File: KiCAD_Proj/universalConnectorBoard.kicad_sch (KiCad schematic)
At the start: 57 parts, among them IC1 RPI_Pico_EvaluationBoard, IC2 SN74LV4052ADR, IC4 TCA9534DWR, J1 691401700003B, J10 Cheeks, J11 MD_SW1, J12 MD_SW2, J13 Motor1, J14 Motor2, J15 Extra VCC/GND, J2 Display1, J3 Display2, J4 RPI4, J5 Ledstrip2, J6 Extra MUX_UART, J7 Radar, J8 Ledstrip1, J9 Mouth, Q1 2N7002, Q2 2N7002, Q3 BSS84, SW1 SW_Push

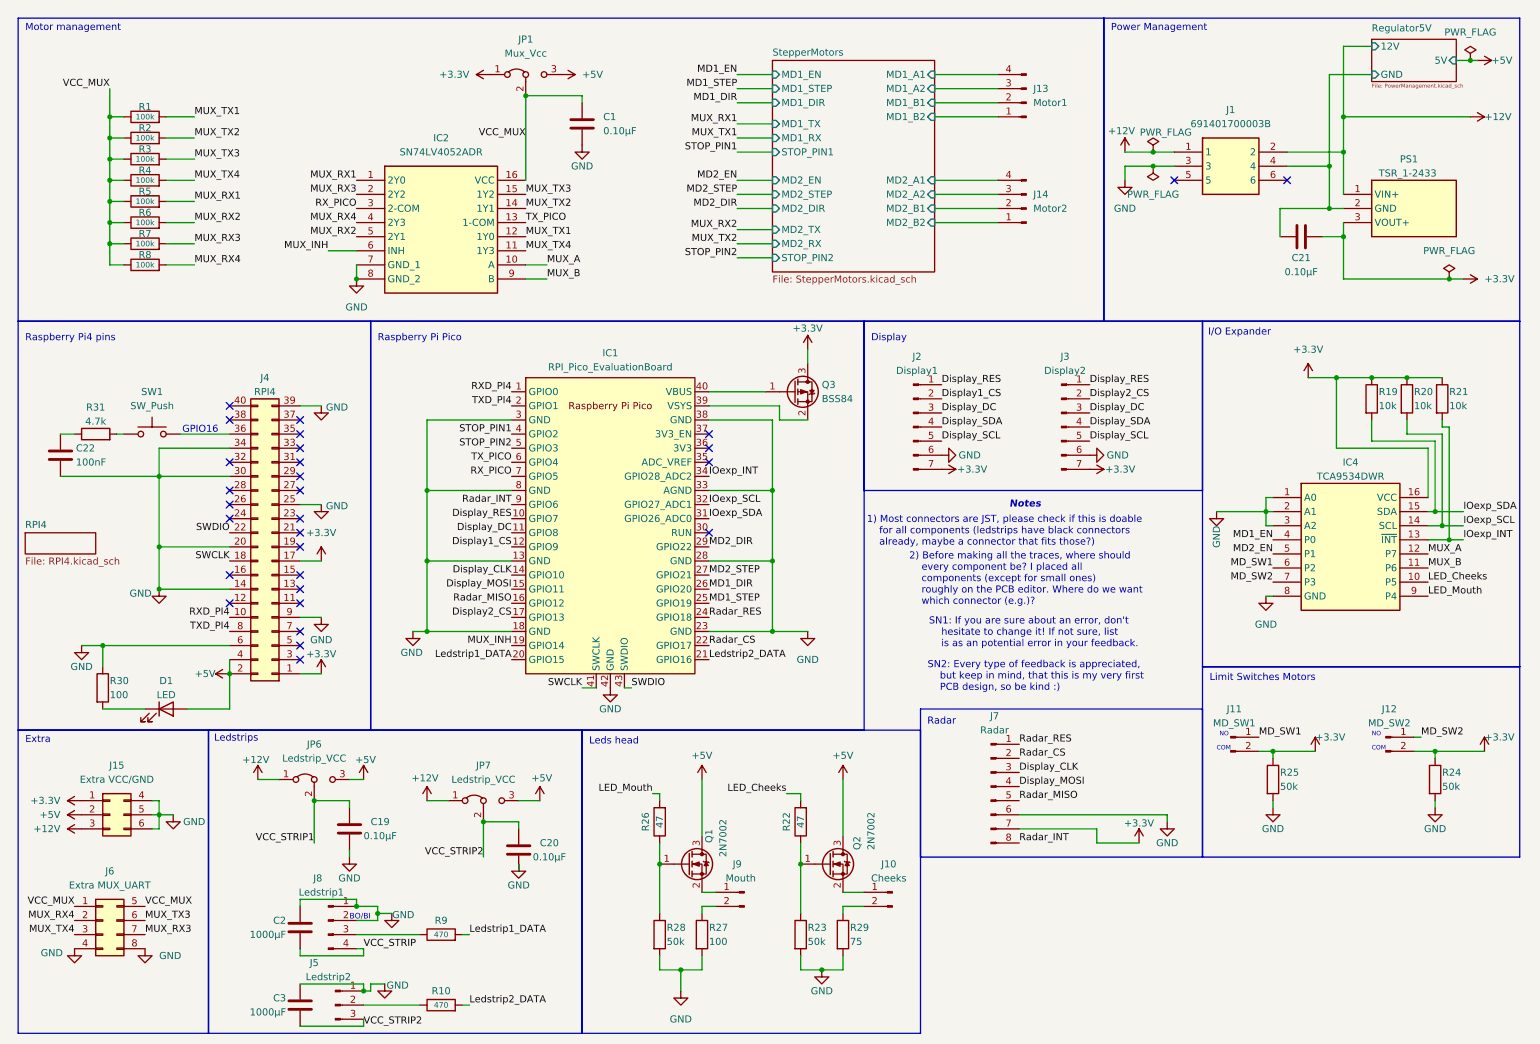
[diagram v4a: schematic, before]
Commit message: Added RPI4 footprint + headers, start of pcb designer
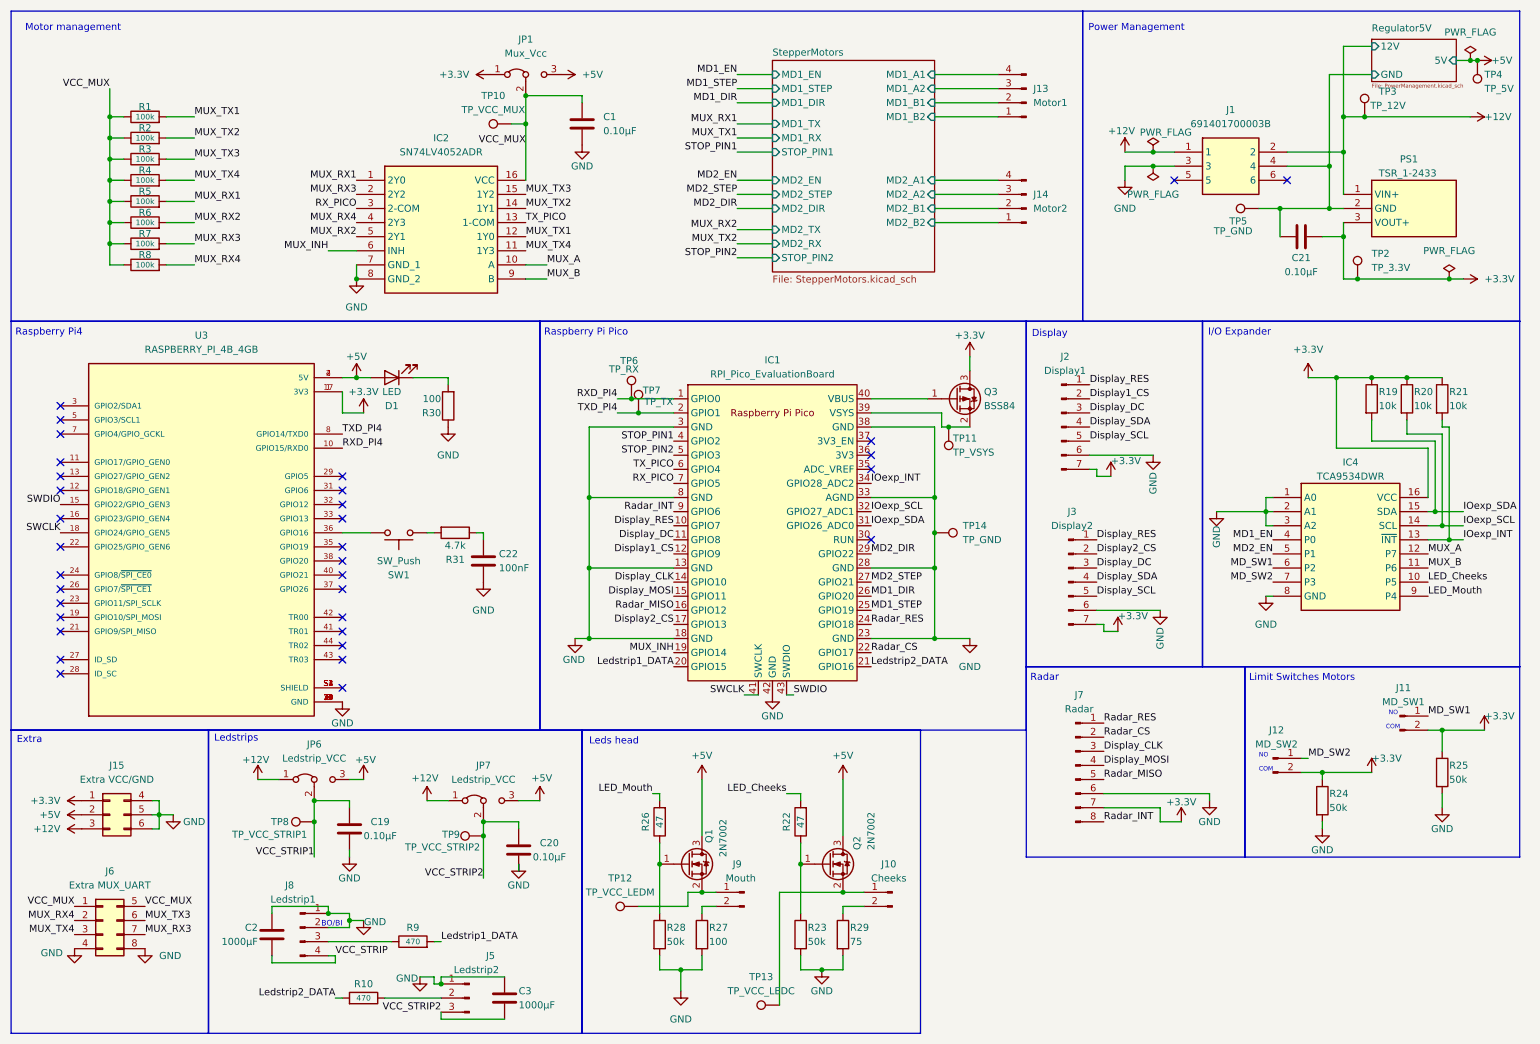
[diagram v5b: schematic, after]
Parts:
- removed J4: RPI4, Connector_PinHeader_2.54mm:PinHeader_2x20_P2.54mm_Vertical, symbol Connector_Generic:Conn_02x20_Odd_Even
- added TP10: TP_VCC_MUX, symbol Connector:TestPoint
- added TP11: TP_VSYS, symbol Connector:TestPoint
- added TP12: TP_VCC_LEDM, symbol Connector:TestPoint
- added TP13: TP_VCC_LEDC, symbol Connector:TestPoint
- added TP14, TP5: TP_GND, symbol Connector:TestPoint
- added TP2: TP_3.3V, symbol Connector:TestPoint
- added TP3: TP_12V, symbol Connector:TestPoint
- added TP4: TP_5V, symbol Connector:TestPoint
- added TP6: TP_RX, symbol Connector:TestPoint
- added TP7: TP_TX, symbol Connector:TestPoint
- added TP8: TP_VCC_STRIP1, symbol Connector:TestPoint
- added TP9: TP_VCC_STRIP2, symbol Connector:TestPoint
- added U3: RASPBERRY_PI_4B_4GB, Healthbot-Footprints:MODULE_RASPBERRY_PI_4B_4GB, symbol Healthbot-Symbols:RASPBERRY_PI_4B_4GB
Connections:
- net +12V: now also TP3.1
- net +3.3V: now also TP2.1, U3.1 (3V3), U3.17 (3V3)
- net +5V: now also TP4.1, U3.2 (5V), U3.4 (5V)
- net GND: now also TP14.1, U3.14 (GND), U3.20 (GND), U3.25 (GND), U3.30 (GND), U3.34 (GND), U3.39 (GND), U3.6 (GND), U3.9 (GND)
- net RXD_PI4: now also TP6.1, U3.10 (GPIO15/RXD0)
- net Regulator5V/GND: now also TP5.1
- net SWCLK: now also U3.18 (GPIO24/GPIO_GEN5)
- net SWDIO: now also U3.15 (GPIO22/GPIO_GEN3)
- net TXD_PI4: now also TP7.1, U3.8 (GPIO14/TXD0)
- net VCC_MUX: now also TP10.1
- net VCC_STRIP1: now also TP8.1
- net VCC_STRIP2: now also TP9.1
- net at J10.1 (Pin_1), Q2.2 (S): now also TP13.1
- net at IC1.39 (VSYS), Q3.2 (S): now also TP11.1
- net at J9.1 (Pin_1), Q1.2 (S): now also TP12.1
- net at SW1.2: now also U3.36 (GPIO16)
- new net: U3.S1 (SHIELD), U3.S2 (SHIELD), U3.S3 (SHIELD), U3.S4 (SHIELD)
- no-connect marks 29 -> 34
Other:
- removed sheet RPI4
- note added: "Raspberry Pi4"
- note removed: "1) Most connectors are JST, please check if this is doable for all components (ledstrips have black connectors already, maybe a connector that fits those?)"
- note removed: "2) Before making all the traces, where should every component be? I placed all components (except for small ones) roughly on the PCB editor. Where do we want which connector (e.g.)?"
- note removed: "GPIO16"
- note removed: "Notes"
- note removed: "Raspberry Pi4 pins"
- note removed: "SN1: If you are sure about an error, don't hesitate to change it! If not sure, list is as an potential error in your feedback."
- note removed: "SN2: Every type of feedback is appreciated, but keep in mind, that this is my very first PCB design, so be kind :)"
- moved on the sheet: C2, C3, IC1, J11, J12, J2, J3, J5, J7, J8, Q3, R10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

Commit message: All components placed
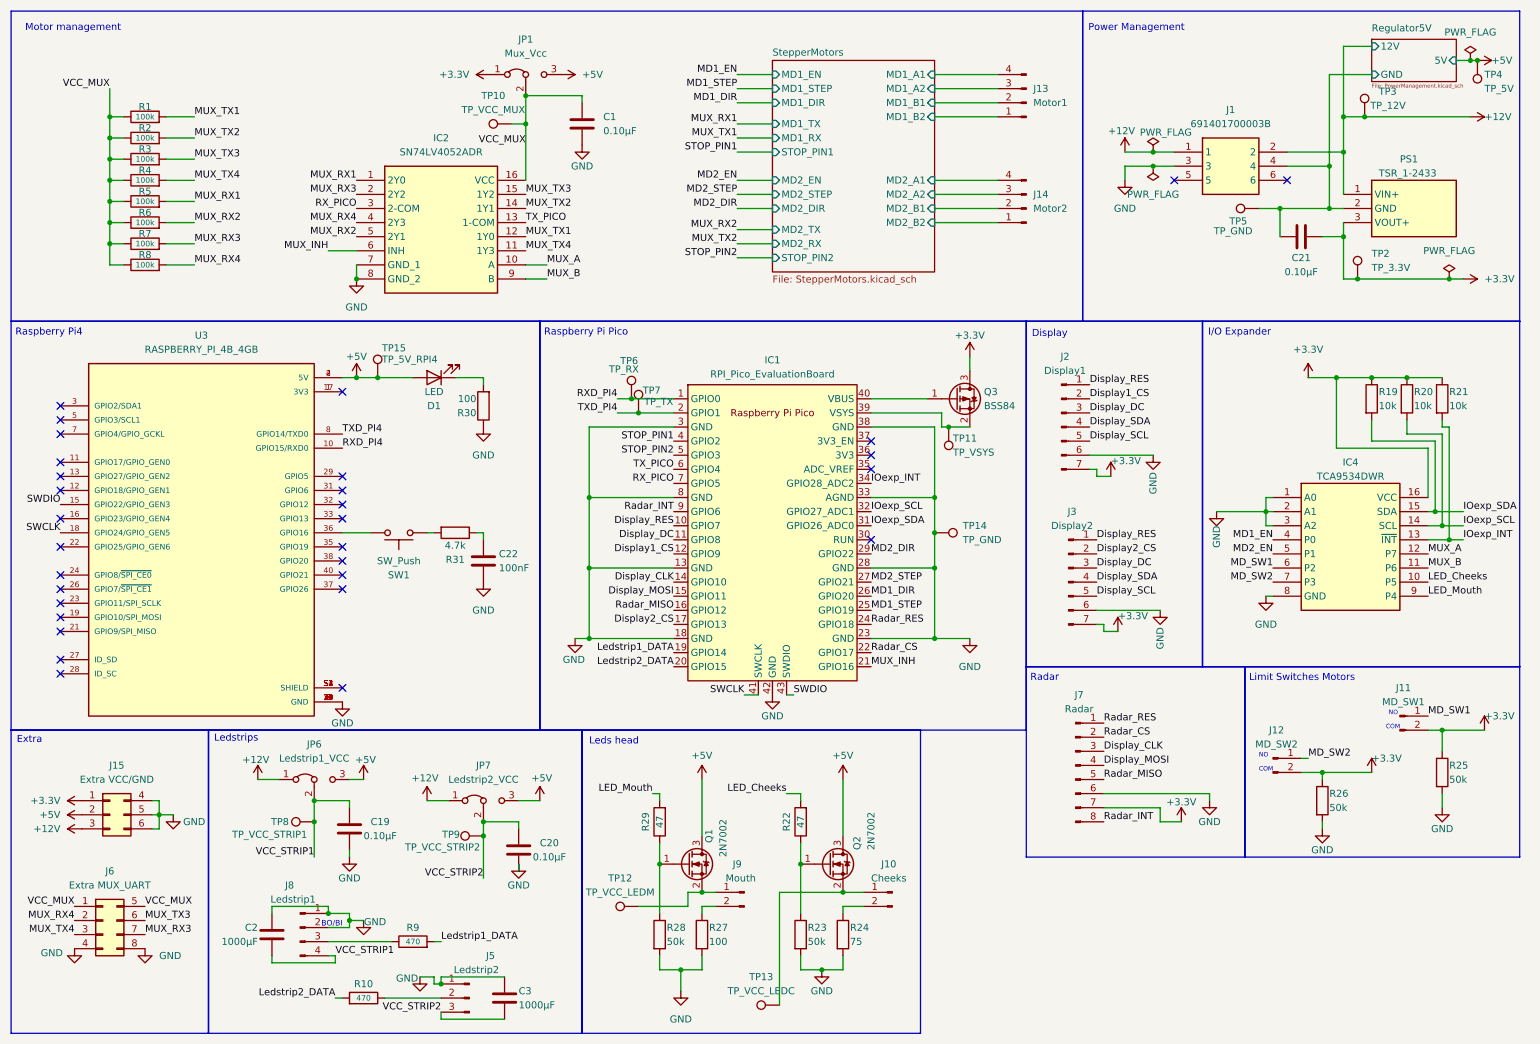
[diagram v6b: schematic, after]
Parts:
- added TP15: TP_5V_RPI4, TestPoint:TestPoint_Pad_D1.5mm, symbol Connector:TestPoint
- JP6: value Ledstrip_VCC -> Ledstrip1_VCC
- JP7: value Ledstrip_VCC -> Ledstrip2_VCC
- PS1: footprint SamacSys_Parts:TSR-1-2433 -> TSR-1-2433
- TP10, TP11, TP12, TP13, TP14, TP2, TP3, TP4, TP5, TP6, TP7, TP8, TP9: footprint (none) -> TestPoint:TestPoint_Pad_D1.5mm
- renumbered R29 to R24, R24 to R26, R26 to R29
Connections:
- net VCC_STRIP is gone; now on net VCC_STRIP1: C2.2, J8.4 (Pin_4)
- net +3.3V: no longer U3.1 (3V3), U3.17 (3V3)
- net +5V: now also TP15.1
- net Ledstrip1_DATA: now also IC1.19 (GPIO14); no longer IC1.20 (GPIO15)
- net Ledstrip2_DATA: now also IC1.20 (GPIO15); no longer IC1.21 (GPIO16)
- net MUX_INH: now also IC1.21 (GPIO16); no longer IC1.19 (GPIO14)
- new net: U3.1 (3V3), U3.17 (3V3)
- no-connect marks 34 -> 31
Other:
- moved on the sheet: D1, R30

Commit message: Nearly finished, just some DRC Errors te check
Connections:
- net Display_SCL is gone; now on net Display_CLK: J2.5 (Pin_5), J3.5 (Pin_5)
- net Display_SDA is gone; now on net Display_MOSI: J2.4 (Pin_4), J3.4 (Pin_4)
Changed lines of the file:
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@@
 		)
 	)
-	(label "Display_SDA"
+	(label "Display_MOSI"
 		(at 208.28 115.57 0)
 		(fields_autoplaced yes)
@@
 		)
 	)
-	(label "Display_SCL"
+	(label "Display_CLK"
 		(at 207.01 90.17 0)
 		(fields_autoplaced yes)
@@
 		)
 	)
-	(label "Display_SDA"
+	(label "Display_MOSI"
 		(at 207.01 87.63 0)
 		(fields_autoplaced yes)
@@
 		)
 	)
-	(label "Display_SCL"
+	(label "Display_CLK"
 		(at 208.28 118.11 0)
 		(fields_autoplaced yes)

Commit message: Finished!
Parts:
- PS1: footprint TSR-1-2433 -> Healthbot-Footprints:TSR-1-2433
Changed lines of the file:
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@@
 			)
 		)
-		(property "Footprint" "TSR-1-2433"
+		(property "Footprint" "Healthbot-Footprints:TSR-1-2433"
 			(at 274.32 140.64 0)
 			(effects
